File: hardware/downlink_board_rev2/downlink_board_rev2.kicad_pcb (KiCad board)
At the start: 2 copper layers, 65 x 56 mm, 53 parts, among them J1 USB_C_Receptacle_USB2.0, J2 SCREEN, J3 GPIO, J6 Conn_ST_STDC14, SW1 RPi_{ON}, SW2 RPi_{OFF}, SW3 MCU_{RST}, U1 AZ1117-3.3, U2 TPS563208DDCR, U3 STM32F103C8Tx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

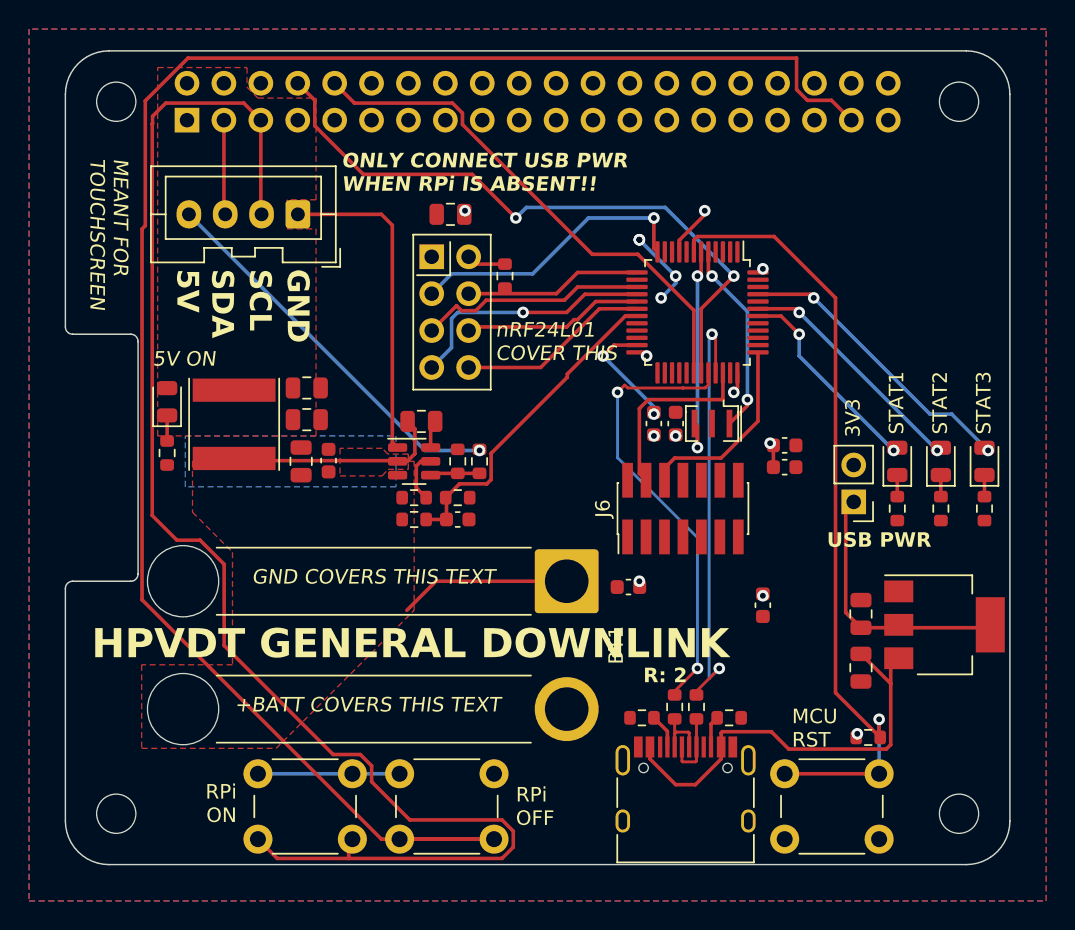
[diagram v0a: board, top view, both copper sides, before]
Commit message: Update on reroutes
Updated the routing such that the routes doesn't go to the edge of the board just in case.
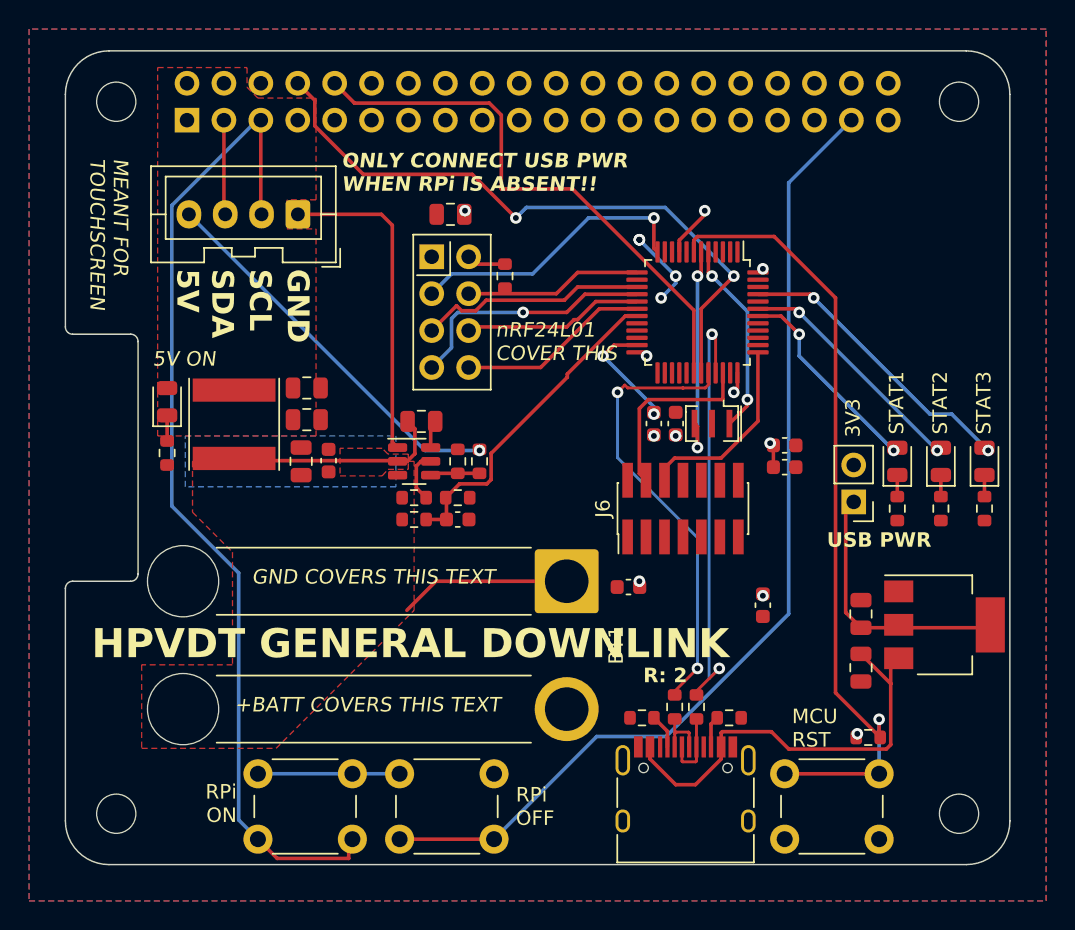
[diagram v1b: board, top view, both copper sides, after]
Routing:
- net /GPIO26: track 124.8 -> 69.0 mm
- net /SCL: track 101.0 -> 69.3 mm
- net /RPi_{RX}: track 36.0 -> 38.5 mm
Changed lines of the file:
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@@
-	)
-	(segment
-		(start 120.298833 92.425)
-		(end 121.075 93.201167)
-		(width 0.25)
-		(layer "F.Cu")
-		(net 3)
-	)
-	(segment
-		(start 118.425 92.425)
-		(end 120.298833 92.425)
-		(width 0.25)
-		(layer "F.Cu")
-		(net 3)
-	)
-	(segment
-		(start 121.075 93.201167)
-		(end 121.075 94.298833)
-		(width 0.25)
-		(layer "F.Cu")
-		(net 3)
 	)
 	(segment
@@
 	)
 	(segment
-		(start 121.075 94.298833)
-		(end 123.701167 96.925)
-		(width 0.25)
-		(layer "F.Cu")
-		(net 3)
-	)
-	(segment
-		(start 130.048833 99.575)
-		(end 119.5 99.575)
-		(width 0.25)
-		(layer "F.Cu")
-		(net 3)
-	)
-	(segment
 		(start 113.45 48.77)
 		(end 113.45 55.2)
@@
 	)
 	(segment
-		(start 110.925 84.925)
-		(end 118.425 92.425)
-		(width 0.25)
-		(layer "F.Cu")
-		(net 3)
-	)
-	(segment
-		(start 107.675 77.675)
-		(end 109.270153 77.675)
-		(width 0.25)
-		(layer "F.Cu")
-		(net 3)
-	)
-	(segment
-		(start 110.925 79.329847)
-		(end 110.925 84.925)
-		(width 0.25)
-		(layer "F.Cu")
-		(net 3)
-	)
-	(segment
-		(start 112.275 47.595)
-		(end 106.905 47.595)
-		(width 0.25)
-		(layer "F.Cu")
-		(net 3)
-	)
-	(segment
-		(start 106 48.5)
-		(end 106 49)
-		(width 0.25)
-		(layer "F.Cu")
-		(net 3)
-	)
-	(segment
-		(start 130.825 98.798833)
-		(end 130.048833 99.575)
-		(width 0.25)
-		(layer "F.Cu")
-		(net 3)
-	)
-	(segment
-		(start 123.701167 96.925)
-		(end 130.048833 96.925)
-		(width 0.25)
-		(layer "F.Cu")
-		(net 3)
-	)
-	(segment
-		(start 130.048833 96.925)
-		(end 130.825 97.701167)
-		(width 0.25)
-		(layer "F.Cu")
-		(net 3)
-	)
-	(segment
 		(start 119.5 98.5)
 		(end 119.5 99.575)
@@
 	)
 	(segment
-		(start 106.905 47.595)
-		(end 106 48.5)
-		(width 0.25)
-		(layer "F.Cu")
-		(net 3)
-	)
-	(segment
-		(start 106 49)
-		(end 105.975 49.025)
-		(width 0.25)
-		(layer "F.Cu")
-		(net 3)
-	)
-	(segment
-		(start 105.975 49.025)
-		(end 105.975 75.975)
-		(width 0.25)
-		(layer "F.Cu")
+		(start 107.325 75.325)
+		(end 111.925 79.925)
+		(width 0.25)
+		(layer "B.Cu")
 		(net 3)
 	)
 	(segment
 		(start 113.45 48.77)
-		(end 112.275 47.595)
-		(width 0.25)
-		(layer "F.Cu")
-		(net 3)
-	)
-	(segment
-		(start 130.825 97.701167)
-		(end 130.825 98.798833)
-		(width 0.25)
-		(layer "F.Cu")
-		(net 3)
-	)
-	(segment
-		(start 105.975 75.975)
-		(end 107.675 77.675)
-		(width 0.25)
-		(layer "F.Cu")
-		(net 3)
-	)
-	(segment
-		(start 109.270153 77.675)
-		(end 110.925 79.329847)
-		(width 0.25)
-		(layer "F.Cu")
+		(end 113.193299 48.77)
+		(width 0.25)
+		(layer "B.Cu")
+		(net 3)
+	)
+	(segment
+		(start 113.193299 48.77)
+		(end 107.325 54.638299)
+		(width 0.25)
+		(layer "B.Cu")
+		(net 3)
+	)
+	(segment
+		(start 107.325 54.638299)
+		(end 107.325 75.325)
+		(width 0.25)
+		(layer "B.Cu")
+		(net 3)
+	)
+	(segment
+		(start 111.925 79.925)
+		(end 111.925 96.925)
+		(width 0.25)
+		(layer "B.Cu")
+		(net 3)
+	)
+	(segment
+		(start 111.925 96.925)
+		(end 113.25 98.25)
+		(width 0.25)
+		(layer "B.Cu")
 		(net 3)
 	)
@@
 	)
 	(segment
-		(start 126.636701 47.595)
-		(end 127.325 48.283299)
+		(start 118.53 46.23)
+		(end 119.895 47.595)
+		(width 0.25)
+		(layer "F.Cu")
+		(net 22)
+	)
+	(segment
+		(start 119.895 47.595)
+		(end 129.176701 47.595)
+		(width 0.25)
+		(layer "F.Cu")
+		(net 22)
+	)
+	(segment
+		(start 129.176701 47.595)
+		(end 130 48.418299)
+		(width 0.25)
+		(layer "F.Cu")
+		(net 22)
+	)
+	(segment
+		(start 134.892764 53.5)
+		(end 143.25 61.857236)
+		(width 0.25)
+		(layer "F.Cu")
+		(net 22)
+	)
+	(segment
+		(start 130 48.418299)
+		(end 130 53.5)
+		(width 0.25)
+		(layer "F.Cu")
+		(net 22)
+	)
+	(segment
+		(start 130 53.5)
+		(end 134.892764 53.5)
 		(width 0.25)
 		(layer "F.Cu")
@@
 	)
 	(segment
-		(start 118.53 46.23)
-		(end 119.895 47.595)
-		(width 0.25)
-		(layer "F.Cu")
-		(net 22)
-	)
-	(segment
-		(start 139.392764 58)
-		(end 143.25 61.857236)
-		(width 0.25)
-		(layer "F.Cu")
-		(net 22)
-	)
-	(segment
-		(start 119.895 47.595)
-		(end 126.636701 47.595)
-		(width 0.25)
-		(layer "F.Cu")
-		(net 22)
-	)
-	(segment
-		(start 136.258299 58)
-		(end 139.392764 58)
-		(width 0.25)
-		(layer "F.Cu")
-		(net 22)
-	)
-	(segment
-		(start 127.325 48.283299)
-		(end 127.325 49.066701)
-		(width 0.25)
-		(layer "F.Cu")
-		(net 22)
-	)
-	(segment
-		(start 127.325 49.066701)
-		(end 136.258299 58)
-		(width 0.25)
-		(layer "F.Cu")
-		(net 22)
-	)
-	(segment
-		(start 150.32 44.5)
-		(end 108.438299 44.5)
-		(width 0.25)
-		(layer "F.Cu")
-		(net 23)
-	)
-	(segment
-		(start 105.5 47.438299)
-		(end 105.5 56.031701)
-		(width 0.25)
-		(layer "F.Cu")
-		(net 23)
-	)
-	(segment
-		(start 152.725 47.405)
-		(end 151.063299 47.405)
-		(width 0.25)
-		(layer "F.Cu")
-		(net 23)
-	)
-	(segment
-		(start 150.32 46.661701)
-		(end 150.32 44.5)
-		(width 0.25)
-		(layer "F.Cu")
-		(net 23)
-	)
-	(segment
-		(start 108.438299 44.5)
-		(end 105.5 47.438299)
-		(width 0.25)
-		(layer "F.Cu")
-		(net 23)
-	)
-	(segment
-		(start 151.063299 47.405)
-		(end 150.32 46.661701)
-		(width 0.25)
-		(layer "F.Cu")
-		(net 23)
-	)
-	(segment
-		(start 154.09 48.77)
-		(end 152.725 47.405)
-		(width 0.25)
-		(layer "F.Cu")
-		(net 23)
-	)
-	(segment
-		(start 105.275 81.775)
-		(end 121.75 98.25)
-		(width 0.25)
-		(layer "F.Cu")
-		(net 23)
-	)
-	(segment
-		(start 121.75 98.25)
-		(end 129.5 98.25)
-		(width 0.25)
-		(layer "F.Cu")
-		(net 23)
-	)
-	(segment
-		(start 105.275 56.256701)
-		(end 105.275 81.775)
-		(width 0.25)
-		(layer "F.Cu")
-		(net 23)
-	)
-	(segment
 		(start 129.5 98.25)
 		(end 123 98.25)
@@
 	)
 	(segment
-		(start 105.5 56.031701)
-		(end 105.275 56.256701)
-		(width 0.25)
-		(layer "F.Cu")
+		(start 149.775 53.085)
+		(end 149.775 82.750305)
+		(width 0.25)
+		(layer "B.Cu")
 		(net 23)
 	)
+	(segment
+		(start 141.33986 91.185445)
+		(end 136.564555 91.185445)
+		(width 0.25)
+		(layer "B.Cu")
+		(net 23)
+	)
+	(segment
+		(start 136.564555 91.185445)
+		(end 129.5 98.25)
+		(width 0.25)
+		(layer "B.Cu")
+		(net 23)
+	)
+	(segment
+		(start 149.775 82.750305)
+		(end 141.33986 91.185445)
+		(width 0.25)
+		(layer "B.Cu")
+		(net 23)
+	)
+	(segment
+		(start 154.09 48.77)
+		(end 149.775 53.085)
+		(width 0.25)
+		(layer "B.Cu")
+		(net 23)
+	)
